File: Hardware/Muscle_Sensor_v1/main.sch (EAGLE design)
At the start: 33 parts, among them IC1 TL084D, IC2 TL7660D, IC3 LM358D, U1 AD8221AR

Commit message: Muscle_Sensor_v1 schematic fixes
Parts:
- added C6, C7: 100n, rcl:C-EUC0805
- R11, R12, R13: value 470R -> 330R
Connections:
- net GND: now also C6.2, C7.2
- net V+: now also C6.1, C7.1
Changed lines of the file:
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@@
 <part name="SJ2" library="jumper" library_urn="urn:adsk.eagle:library:252" deviceset="SJ" device="" package3d_urn="urn:adsk.eagle:package:15471/1"/>
 <part name="SJ3" library="jumper" library_urn="urn:adsk.eagle:library:252" deviceset="SJ" device="" package3d_urn="urn:adsk.eagle:package:15471/1"/>
-<part name="R11" library="rcl" library_urn="urn:adsk.eagle:library:334" deviceset="R-EU_" device="R1206" package3d_urn="urn:adsk.eagle:package:23540/2" value="470R"/>
-<part name="R12" library="rcl" library_urn="urn:adsk.eagle:library:334" deviceset="R-EU_" device="R1206" package3d_urn="urn:adsk.eagle:package:23540/2" value="470R"/>
+<part name="R11" library="rcl" library_urn="urn:adsk.eagle:library:334" deviceset="R-EU_" device="R1206" package3d_urn="urn:adsk.eagle:package:23540/2" value="330R"/>
+<part name="R12" library="rcl" library_urn="urn:adsk.eagle:library:334" deviceset="R-EU_" device="R1206" package3d_urn="urn:adsk.eagle:package:23540/2" value="330R"/>
 <part name="LED1" library="led" library_urn="urn:adsk.eagle:library:259" deviceset="LED" device="CHIP-LED0805" package3d_urn="urn:adsk.eagle:package:15818/2"/>
 <part name="LED2" library="led" library_urn="urn:adsk.eagle:library:259" deviceset="LED" device="CHIP-LED0805" package3d_urn="urn:adsk.eagle:package:15818/2"/>
@@
 <part name="P+5" library="supply1" library_urn="urn:adsk.eagle:library:371" deviceset="V+" device=""/>
 <part name="GND13" library="supply1" library_urn="urn:adsk.eagle:library:371" deviceset="GND" device=""/>
-<part name="R13" library="rcl" library_urn="urn:adsk.eagle:library:334" deviceset="R-EU_" device="R1206" package3d_urn="urn:adsk.eagle:package:23540/2" value="470R"/>
+<part name="R13" library="rcl" library_urn="urn:adsk.eagle:library:334" deviceset="R-EU_" device="R1206" package3d_urn="urn:adsk.eagle:package:23540/2" value="330R"/>
 <part name="LED3" library="led" library_urn="urn:adsk.eagle:library:259" deviceset="LED" device="CHIP-LED0805" package3d_urn="urn:adsk.eagle:package:15818/2"/>
+<part name="C6" library="rcl" library_urn="urn:adsk.eagle:library:334" deviceset="C-EU" device="C0805" package3d_urn="urn:adsk.eagle:package:23617/2" value="100n"/>
+<part name="C7" library="rcl" library_urn="urn:adsk.eagle:library:334" deviceset="C-EU" device="C0805" package3d_urn="urn:adsk.eagle:package:23617/2" value="100n"/>
 </parts>
 <sheets>
@@
 <attribute name="VALUE" x="46.228" y="24.765" size="1.778" layer="96"/>
 </instance>
+<instance part="C6" gate="G$1" x="33.02" y="38.1" smashed="yes">
+<attribute name="NAME" x="34.544" y="38.481" size="1.778" layer="95"/>
+<attribute name="VALUE" x="34.544" y="33.401" size="1.778" layer="96"/>
+</instance>
+<instance part="C7" gate="G$1" x="27.94" y="38.1" smashed="yes">
+<attribute name="NAME" x="29.464" y="38.481" size="1.778" layer="95"/>
+<attribute name="VALUE" x="29.464" y="33.401" size="1.778" layer="96"/>
+</instance>
 </instances>
 <busses>
@@
 <junction x="38.1" y="30.48"/>
 <pinref part="LED3" gate="G$1" pin="C"/>
+<wire x1="38.1" y1="30.48" x2="33.02" y2="30.48" width="0.1524" layer="91"/>
+<pinref part="C6" gate="G$1" pin="2"/>
+<wire x1="33.02" y1="30.48" x2="33.02" y2="33.02" width="0.1524" layer="91"/>
+<pinref part="C7" gate="G$1" pin="2"/>
+<wire x1="27.94" y1="33.02" x2="27.94" y2="30.48" width="0.1524" layer="91"/>
+<wire x1="27.94" y1="30.48" x2="33.02" y2="30.48" width="0.1524" layer="91"/>
+<junction x="33.02" y="30.48"/>
 </segment>
 </net>
@@
 <junction x="38.1" y="43.18"/>
 <pinref part="R13" gate="G$1" pin="1"/>
+<wire x1="38.1" y1="43.18" x2="33.02" y2="43.18" width="0.1524" layer="91"/>
+<pinref part="C6" gate="G$1" pin="1"/>
+<wire x1="33.02" y1="43.18" x2="33.02" y2="40.64" width="0.1524" layer="91"/>
+<pinref part="C7" gate="G$1" pin="1"/>
+<wire x1="27.94" y1="40.64" x2="27.94" y2="43.18" width="0.1524" layer="91"/>
+<wire x1="27.94" y1="43.18" x2="33.02" y2="43.18" width="0.1524" layer="91"/>
+<junction x="33.02" y="43.18"/>
 </segment>
 </net>

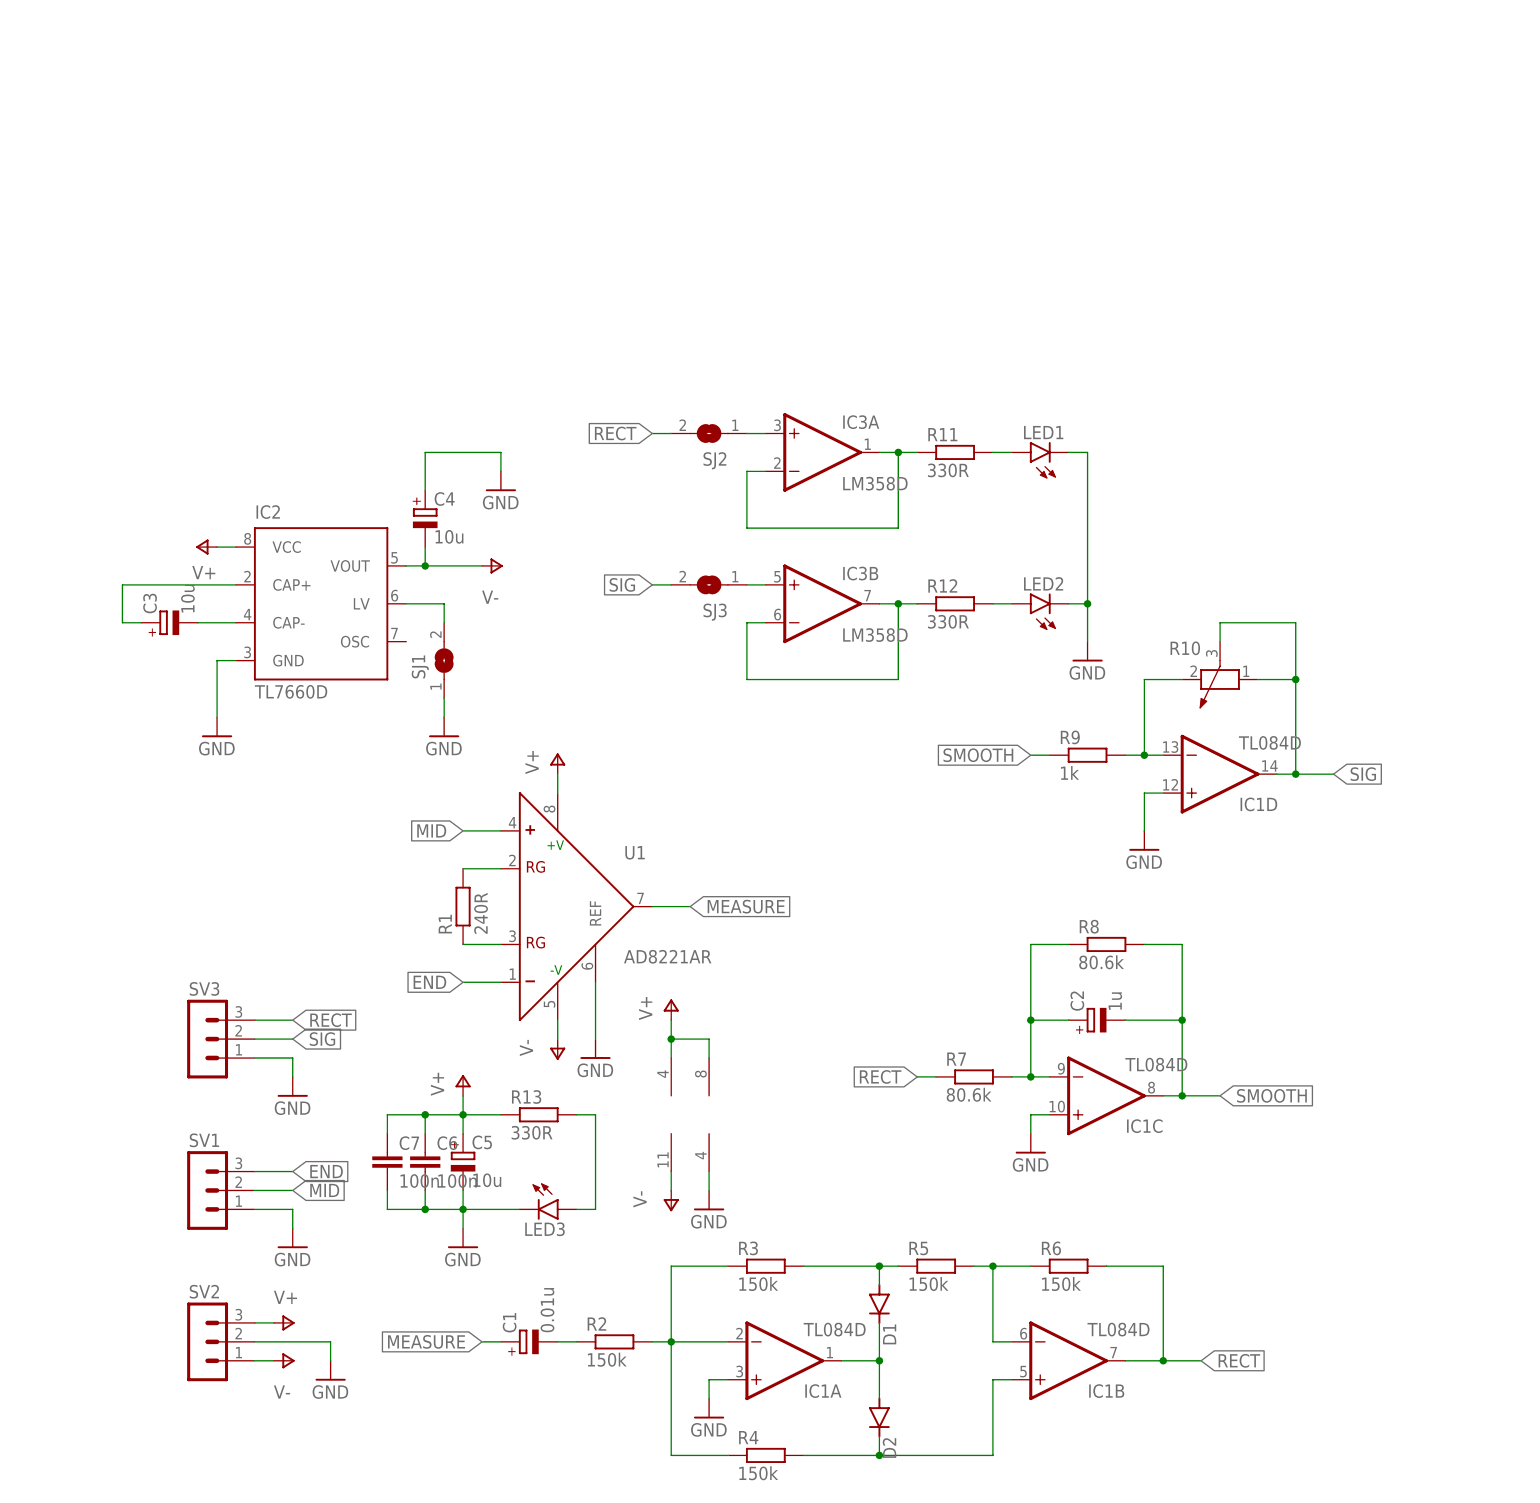
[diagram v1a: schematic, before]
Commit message: Create Muscle_Sensor_v1 board
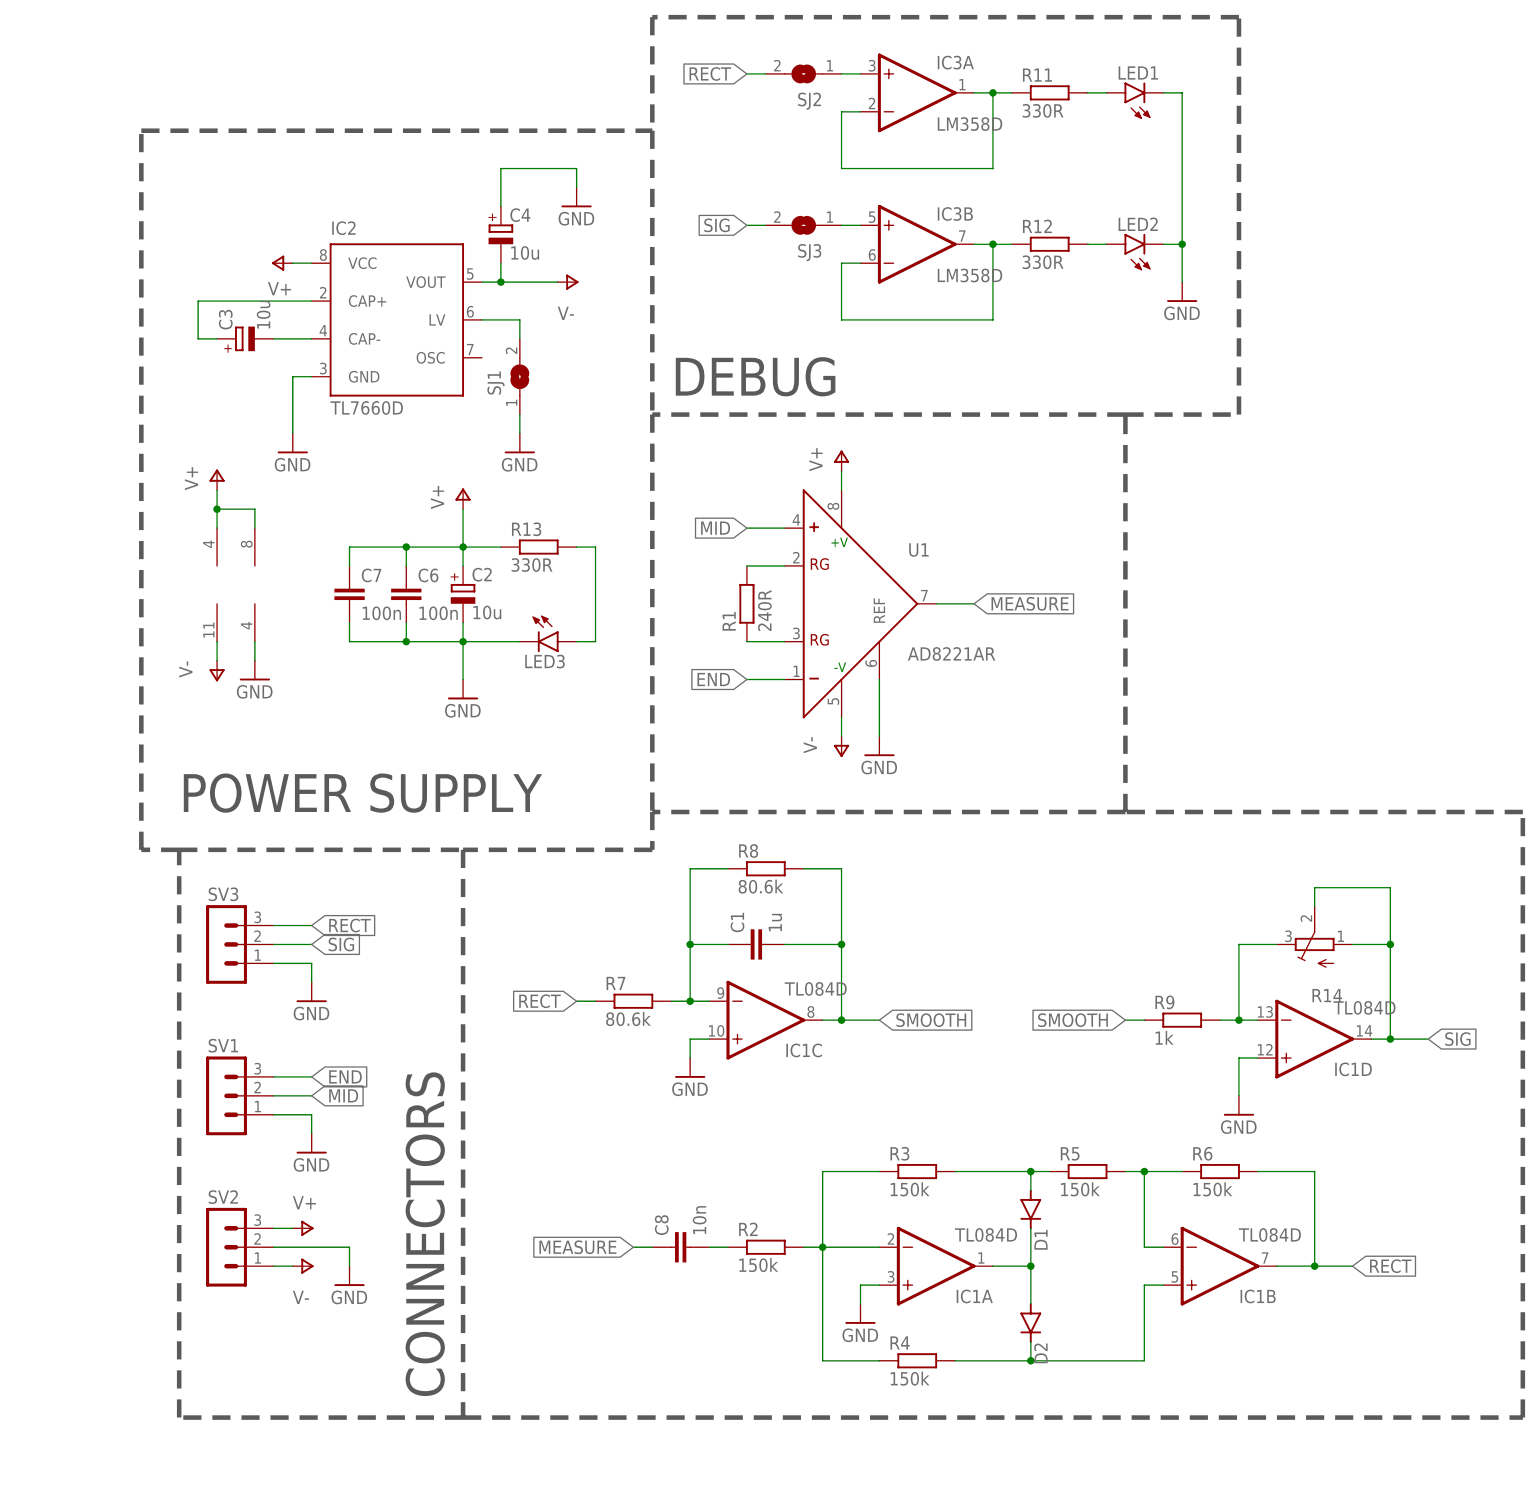
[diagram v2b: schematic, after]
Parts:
- removed C5: 10u, rcl:CPOL-EU085CS-1AR
- removed R10: (no value), rcl:POTENTIOMETER_PT_SPIN
- added C8: 10n, rcl:C-EUC0805
- added R14: (no value), pot:TRIM_EU-SM-42/43B
- C1: value 0.01u -> 1u; device rcl:CPOL-EU085CS-1AR -> rcl:C-EUC0805
- C2: value 1u -> 10u; device rcl:CPOL-EU085CS-1AR -> rcl:CPOL-EUSMCB
- C3, C4: device rcl:CPOL-EU085CS-1AR -> rcl:CPOL-EUSMCB
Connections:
- net GND: now also C2.-; no longer C5.-
- net MEASURE: now also C8.1; no longer C1.+
- net N$11: now also R14.E; no longer R10.2
- net N$2: now also C8.2; no longer C1.-
- net N$9: now also C1.1; no longer C2.+
- net SIG: now also R14.A, R14.S; no longer R10.1, R10.3
- net SMOOTH: now also C1.2; no longer C2.-
- net V+: now also C2.+; no longer C5.+
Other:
- note added: "CONNECTORS"
- note added: "DEBUG"
- note added: "POWER SUPPLY"
- moved on the sheet: C2, C3, C4, C6, C7, D1, D2, IC1A, IC1B, IC1C, IC1D, IC2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

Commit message: Update Muscle_Sensor_v1
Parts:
- removed IC3: LM358D, linear:LM358D
- removed LED1, LED2: (no value), led:LEDCHIP-LED0805
- removed R11, R12: 330R, rcl:R-EU_R1206
- removed R14: (no value), pot:TRIM_EU-SM-42/43B
- removed SJ2, SJ3: (no value), jumper:SJ
- removed SV3: (no value), con-lstb:MA03-1
- added H1, H2: MOUNT-HOLE3.0, holes:MOUNT-HOLE3.0
- added K1, K2: 61000418221, Wurth_Elektronik_Electromechanic_Board_to_Board_Connectors_rev15c:61000418221
- added R10: (no value), rcl:R-TRIMM3314J
- SV2: device con-lstb:MA03-1 -> con-lstb:MA04-1
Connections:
- removed net N$12: IC3A.+IN, SJ2.1
- removed net N$15: IC3B.+IN, SJ3.1
- removed net N$16: IC3B.-IN, IC3B.OUT, R12.1
- removed net N$17: IC3A.-IN, IC3A.OUT, R11.1
- removed net N$18: LED1.A, R11.2
- removed net N$20: LED2.A, R12.2
- net GND: now also K1.2, K1.3, K2.2, K2.3, SV2.1; no longer IC3P.V-, LED1.C, LED2.C, SV2.2, SV3.1
- net N$11: now also R10.E; no longer R14.E
- net RECT: now also SV2.3; no longer SJ2.2, SV3.3
- net SIG: now also R10.A, R10.S, SV2.2; no longer R14.A, R14.S, SJ3.2, SV3.2
- net V+: now also K1.4, K2.4, SV2.4; no longer IC3P.V+, SV2.3
- net V-: now also K1.1, K2.1; no longer SV2.1
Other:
- note removed: "DEBUG"
